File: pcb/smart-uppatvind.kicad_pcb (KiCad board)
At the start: 4 copper layers, 74 x 36 mm, 65 parts, among them J1 PWR, J2 EXT_SENSOR, J3 UART_PROG, J4 FAN, Q1 IRLML9301, Q2 MMBT3904, Q3 MMBT3904, Q4 MMBT3904, Q5 Q_NMOS_GSD, SW1 EN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

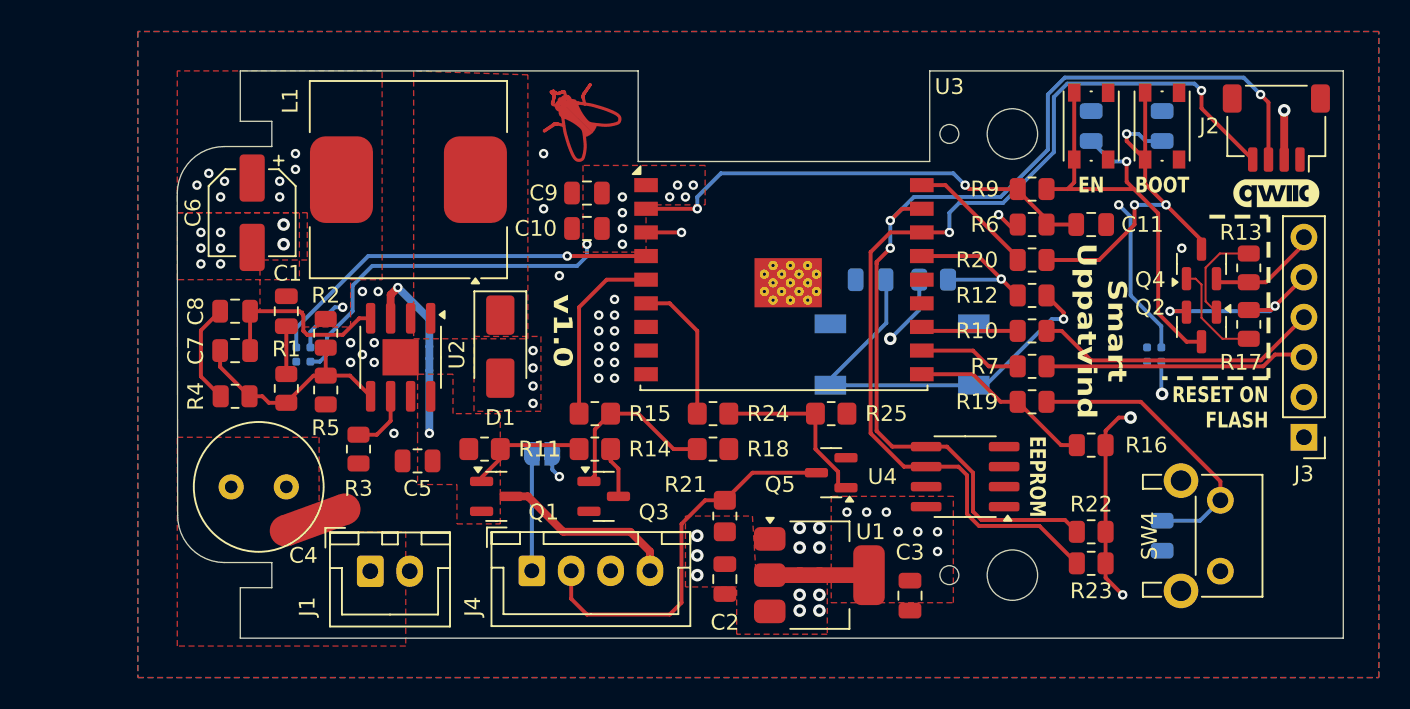
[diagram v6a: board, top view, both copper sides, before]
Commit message: Finishing touches, via stitching
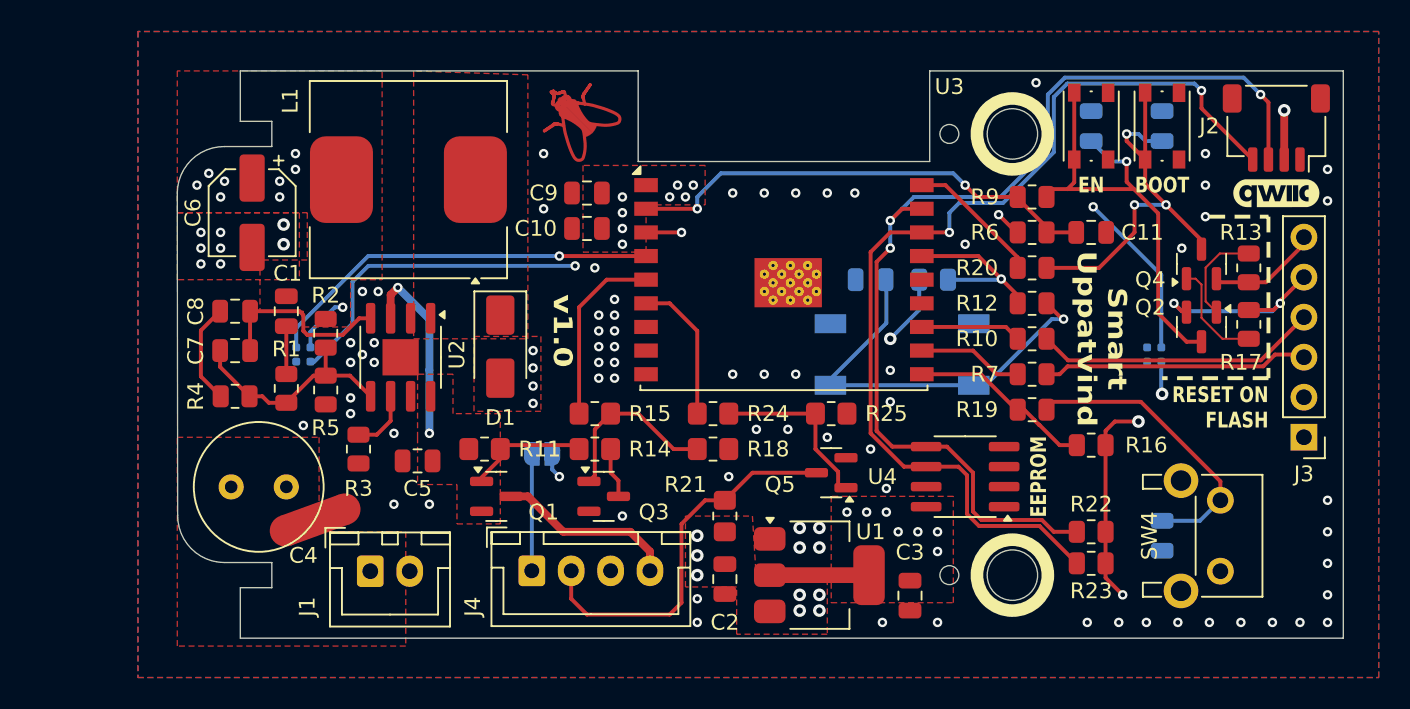
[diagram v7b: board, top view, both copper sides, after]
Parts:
- moved C11 0.50 mm to (111.1, 51.0)
- moved R10 0.50 mm to (107.3, 57.7)
- moved R12 0.50 mm to (107.3, 55.5)
- moved R19 0.50 mm to (107.3, 62.2)
- moved R20 0.50 mm to (107.3, 53.2)
- moved R6 0.50 mm to (107.3, 51.0)
- moved R7 0.50 mm to (107.3, 60.0)
- moved R9 0.50 mm to (107.3, 48.7)
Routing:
- net Net-(C12-Pad2): track 26.7 -> 25.0 mm
- net Net-(D2-DOUT): track 70.6 -> 69.8 mm
- net +5V: track 39.7 -> 39.1 mm
- net GND: vias 27 -> 73

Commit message: Minor adjustments, added missing 3D models
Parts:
- J2: value EXT_SENSOR -> QWIIC
